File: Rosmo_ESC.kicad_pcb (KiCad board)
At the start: 2 copper layers, 50 x 50 mm, 48 parts, among them J1 M-BUS, J2 USB_C_Receptacle_USB2.0, J3 Conn_01x06_MountingPin, J4 Conn_01x06_MountingPin, J5 Conn_01x03, J6 Conn_01x03, J7 Conn_01x02, U1 STM32G474RET6, U2 PRTR5V0U2F, U3 MPS6540H, U4 MPS6540H

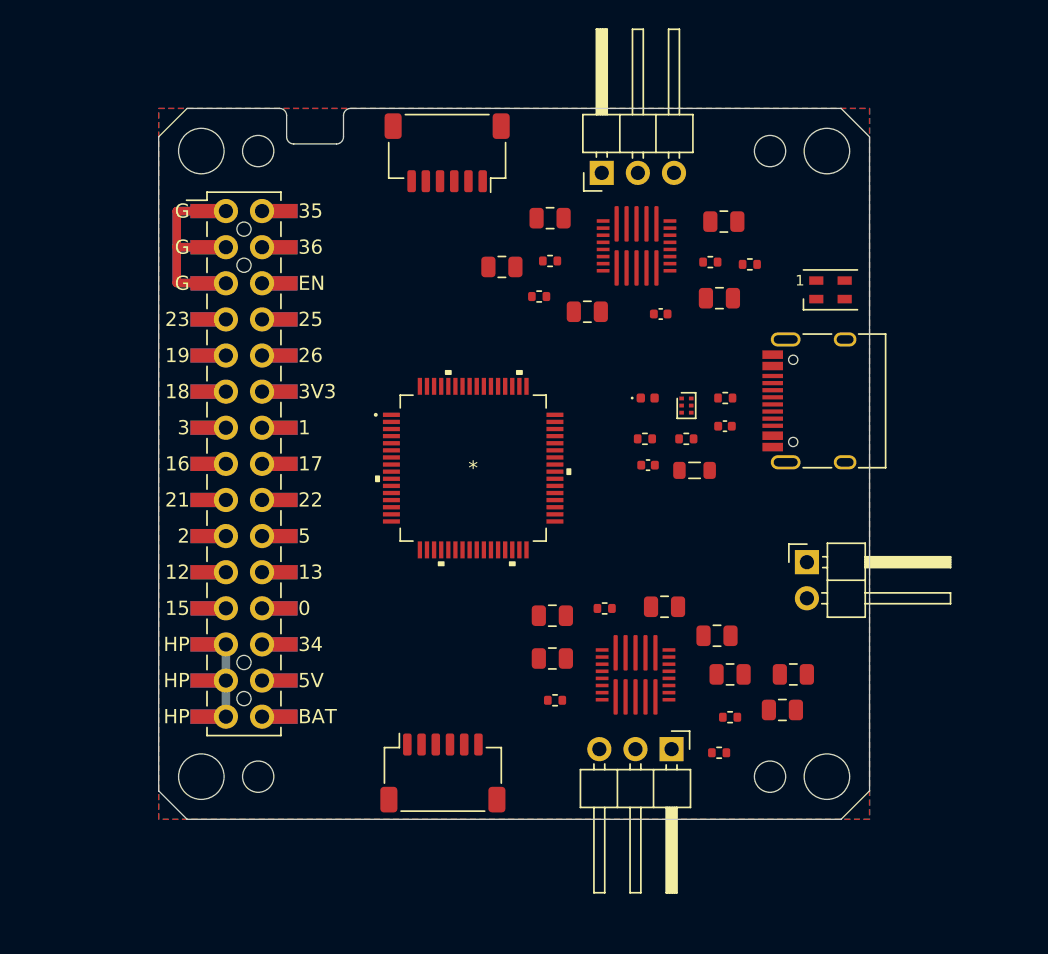
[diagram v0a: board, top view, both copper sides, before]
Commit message: working on rosmo ESC, routing half done
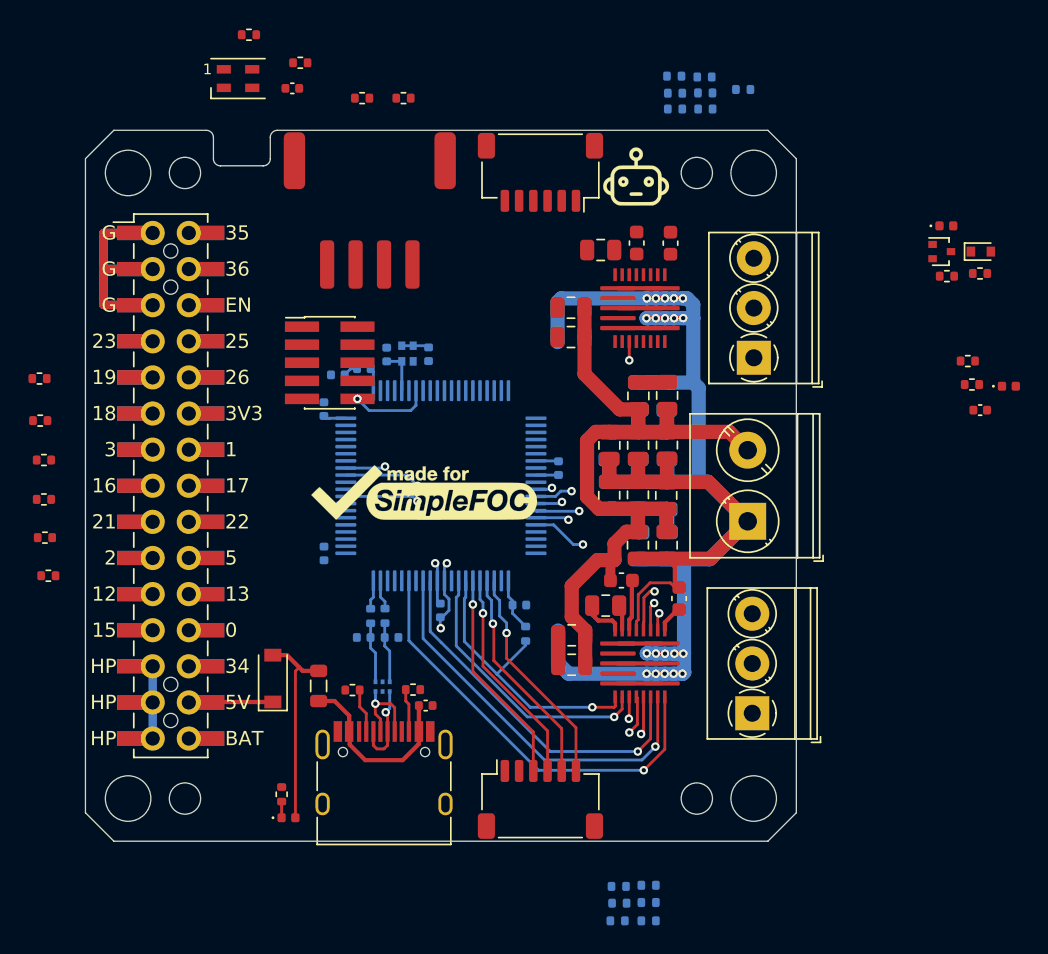
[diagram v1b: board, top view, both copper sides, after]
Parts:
- added C14: 10nF 75V, Capacitor_SMD:C_0805_2012Metric, F.Cu at (84.2, 62.5)
- added C15: 100nF 75V, Capacitor_SMD:C_0805_2012Metric, F.Cu at (84.2, 64.5)
- added C16: 1uF 16V, Capacitor_SMD:C_0603_1608Metric, F.Cu at (88.8, 57.9)
- added C17: 100nF 75V, Capacitor_SMD:C_0805_2012Metric, F.Cu at (86.2, 58.4)
- added C18: 4.7uF 16V, Capacitor_SMD:C_0603_1608Metric, F.Cu at (91.2, 57.9)
- added C19: 10nF 75V, Capacitor_SMD:C_0805_2012Metric, F.Cu at (84.2, 85.5)
- added C20: 100nF 75V, Capacitor_SMD:C_0805_2012Metric, F.Cu at (84.2, 87.6)
- added C21: 1uF 16V, Capacitor_SMD:C_0603_1608Metric, F.Cu at (87.7, 81.7)
- added C22: 100nF 75V, Capacitor_SMD:C_0805_2012Metric, F.Cu at (86.6, 83.4)
- added C23: 4.7uF 16V, Capacitor_SMD:C_0603_1608Metric, F.Cu at (91.8, 82.9)
- added C24: 100nF 6.3V, Capacitor_SMD:C_0402_1005Metric, B.Cu at (74.1, 65.8)
- added C25: 10uF 50V, Capacitor_SMD:C_0805_2012Metric, B.Cu at (90.9, 68.7)
- added C26: 10uF 50V, Capacitor_SMD:C_0805_2012Metric, B.Cu at (88.9, 68.7)
- added C27: 10uF 50V, Capacitor_SMD:C_0805_2012Metric, B.Cu at (86.8, 75.7)
- added C28: 10uF 50V, Capacitor_SMD:C_0805_2012Metric, F.Cu at (88.9, 68.7)
- added C29: 10uF 50V, Capacitor_SMD:C_0805_2012Metric, F.Cu at (90.9, 68.7)
- added C30: 10uF 50V, Capacitor_SMD:C_0805_2012Metric, B.Cu at (90.9, 79.2)
- added C31: 10uF 50V, Capacitor_SMD:C_0805_2012Metric, B.Cu at (90.9, 75.7)
- added C32: 10uF 50V, Capacitor_SMD:C_0805_2012Metric, B.Cu at (88.9, 75.7)
- added C33: 10uF 50V, Capacitor_SMD:C_0805_2012Metric, F.Cu at (86.8, 75.7)
- added C34: 10uF 50V, Capacitor_SMD:C_0805_2012Metric, F.Cu at (88.9, 75.6)
- added C35: 10uF 50V, Capacitor_SMD:C_0805_2012Metric, F.Cu at (90.8, 75.7)
- added C36: 10uF 50V, Capacitor_SMD:C_0805_2012Metric, B.Cu at (88.9, 79.2)
- added C37: 10uF 50V, Capacitor_SMD:C_0805_2012Metric, B.Cu at (86.8, 72.2)
- added C38: 10uF 50V, Capacitor_SMD:C_0805_2012Metric, F.Cu at (88.9, 79.2)
- added C39: 10uF 50V, Capacitor_SMD:C_0805_2012Metric, F.Cu at (90.9, 79.2)
- added C40: 10uF 50V, Capacitor_SMD:C_0805_2012Metric, F.Cu at (90.9, 72.1)
- added C41: 10uF 50V, Capacitor_SMD:C_0805_2012Metric, F.Cu at (88.9, 72.2)
- added C42: 10uF 50V, Capacitor_SMD:C_0805_2012Metric, F.Cu at (86.8, 72.2)
- added C43: 10uF 50V, Capacitor_SMD:C_0805_2012Metric, B.Cu at (88.9, 72.2)
- added C44: 10uF 50V, Capacitor_SMD:C_0805_2012Metric, B.Cu at (90.9, 72.2)
- added D3: green, LED_SMD:LED_0402_1005Metric, F.Cu at (110.5, 56.7)
- added D4: SK6805, LED_SMD:LED_SK6805_PLCC4_2.4x2.7mm_P1.3mm, F.Cu at (60.7, 46.4)
- added D5: SC1333-01ETG, Diode_SMD:D_0402_1005Metric, F.Cu at (115.0, 68.0)
- added D6: 2.84V, Diode_SMD:D_SOD-523, F.Cu at (113.0, 58.5)
- added J8: Conn_01x03, TerminalBlock_Phoenix:TerminalBlock_Phoenix_PT-1,5-3-3.5-H_1x03_P3.50mm_Horizontal, F.Cu at (96.9, 91.0)
- added J9: Conn_01x02, TerminalBlock_Phoenix:TerminalBlock_Phoenix_PT-1,5-2-5.0-H_1x02_P5.00mm_Horizontal, F.Cu at (96.6, 77.5)
- added L1: SimpleFOC_Logo, runger:MadeForSimpleFOC_16mm, F.Cu at (73.8, 75.5)
- added L2: Robo_Logo, runger:Robo_logo2, F.Cu at (88.7, 53.2)
- added L3: Logo_Open_Hardware_Small, Symbol:OSHW-Symbol_6.7x6mm_SilkScreen, B.Cu at (84.9, 95.5)
- added L4: CC_Logo, runger:CC_Logo_5mm, B.Cu at (89.5, 89.0)
- added L5: CC_Attribution_Logo, runger:CC_Attribution_Logo_5mm, B.Cu at (84.9, 89.0)
- added L6: CC_Sharealike_Logo, runger:CC_Sharealike_Logo_5mm, B.Cu at (80.4, 89.0)
- added Q1: BC847BTT1G, Package_TO_SOT_SMD:SOT-416, F.Cu at (110.2, 58.5)
- added R14: 5k1, Resistor_SMD:R_0402_1005Metric, F.Cu at (65.1, 45.2)
- added R15: 300R, Resistor_SMD:R_0402_1005Metric, F.Cu at (61.5, 43.3)
- added R16: 2.2k 1%, Resistor_SMD:R_0402_1005Metric, F.Cu at (112.1, 66.2)
- added R17: 200Ω, Resistor_SMD:R_0402_1005Metric, F.Cu at (110.6, 60.3)
- added R18: 10k, Resistor_SMD:R_0402_1005Metric, B.Cu at (96.3, 47.1)
- added R19: 2k2 0.5%, Resistor_SMD:R_0402_1005Metric, B.Cu at (93.5, 46.2)
- added R20: 2k2 0.5%, Resistor_SMD:R_0402_1005Metric, B.Cu at (93.6, 47.4)
- added R21: 2k2 0.5%, Resistor_SMD:R_0402_1005Metric, B.Cu at (93.6, 48.5)
- added R22: 2k2 0.5%, Resistor_SMD:R_0402_1005Metric, B.Cu at (91.4, 46.2)
- added R23: 2k2 0.5%, Resistor_SMD:R_0402_1005Metric, B.Cu at (91.5, 47.4)
- added R24: 2k2 0.5%, Resistor_SMD:R_0402_1005Metric, B.Cu at (91.5, 48.5)
- added R25: 10k, Resistor_SMD:R_0402_1005Metric, B.Cu at (81.0, 85.4)
- added R26: 2k2 0.5%, Resistor_SMD:R_0402_1005Metric, B.Cu at (89.6, 103.1)
- added R27: 2k2 0.5%, Resistor_SMD:R_0402_1005Metric, B.Cu at (89.6, 104.3)
- added R28: 2k2 0.5%, Resistor_SMD:R_0402_1005Metric, B.Cu at (89.6, 105.6)
- added R29: 2k2 0.5%, Resistor_SMD:R_0402_1005Metric, B.Cu at (87.5, 103.2)
- added R30: 2k2 0.5%, Resistor_SMD:R_0402_1005Metric, B.Cu at (87.5, 104.4)
- added R31: 2k2 0.5%, Resistor_SMD:R_0402_1005Metric, B.Cu at (87.4, 105.6)
- added R32: 2k2, Resistor_SMD:R_0402_1005Metric, F.Cu at (69.5, 47.7)
- added R33: 2k2, Resistor_SMD:R_0402_1005Metric, F.Cu at (72.4, 47.7)
- added X1: 25MHz, Oscillator:Oscillator_SMD_Abracon_ASCO-4Pin_1.6x1.2mm, B.Cu at (72.7, 65.7)
- C1: value 10nF 10V -> 100nF 6.3V; moved to B.Cu
- C10: value 100nF -> 47pF 10V; footprint Capacitor_SMD:C_0805_2012Metric -> Capacitor_SMD:C_0402_1005Metric; moved to B.Cu
- C11: value 1uF -> 10nF 10V; footprint Capacitor_SMD:C_0805_2012Metric -> Capacitor_SMD:C_0402_1005Metric
- C12: value 100nF -> 100nF 6.3V; footprint Capacitor_SMD:C_0805_2012Metric -> Capacitor_SMD:C_0402_1005Metric
- C13: value 4.7uF -> 100nF 50V 5%; footprint Capacitor_SMD:C_0805_2012Metric -> Capacitor_SMD:C_0402_1005Metric
- C2: value 47pF 10V -> 10pF 6.3V 5%; moved to B.Cu
- C3: value 47pF 10V -> 100nF 6.3V; moved to B.Cu
- C4: value 10nF -> 100nF 6.3V; footprint Capacitor_SMD:C_0805_2012Metric -> Capacitor_SMD:C_0402_1005Metric; moved to B.Cu
- C5, C7: value 100nF -> 100nF 6.3V; footprint Capacitor_SMD:C_0805_2012Metric -> Capacitor_SMD:C_0402_1005Metric; moved to B.Cu
- C6: value 1uF -> 100nF 6.3V; footprint Capacitor_SMD:C_0805_2012Metric -> Capacitor_SMD:C_0402_1005Metric; moved to B.Cu
- C8: value 4.7uF -> 100nF 6.3V; footprint Capacitor_SMD:C_0805_2012Metric -> Capacitor_SMD:C_0402_1005Metric; moved to B.Cu
- C9: value 10nF -> 47pF 10V; footprint Capacitor_SMD:C_0805_2012Metric -> Capacitor_SMD:C_0402_1005Metric; moved to B.Cu
- D1: value green -> PMEG40T10ER; footprint LED_SMD:LED_0402_1005Metric -> Diode_SMD:D_SOD-123
- D2: value SK6805 -> green; footprint LED_SMD:LED_SK6805_PLCC4_2.4x2.7mm_P1.3mm -> LED_SMD:LED_0402_1005Metric
- J3: value Conn_01x06_MountingPin -> Conn_01x04_MountingPin; footprint Connector_JST:JST_SH_SM06B-SRSS-TB_1x06-1MP_P1.00mm_Horizontal -> runger:Grove_A2006WF-04A
- J4: value Conn_01x06_MountingPin -> Conn_02x05; footprint Connector_JST:JST_SH_SM06B-SRSS-TB_1x06-1MP_P1.00mm_Horizontal -> Connector_PinHeader_1.27mm:PinHeader_2x05_P1.27mm_Vertical_SMD
- J5, J6: value Conn_01x03 -> JST_SH_SM06B-SRSS-TB_1x06-1MP; footprint Connector_PinHeader_2.54mm:PinHeader_1x03_P2.54mm_Horizontal -> Connector_JST:JST_SH_SM06B-SRSS-TB_1x06-1MP_P1.00mm_Horizontal
- J7: value Conn_01x02 -> Conn_01x03; footprint Connector_PinHeader_2.54mm:PinHeader_1x02_P2.54mm_Horizontal -> TerminalBlock_Phoenix:TerminalBlock_Phoenix_PT-1,5-3-3.5-H_1x03_P3.50mm_Horizontal
- R1, R2: value 27R -> 2k2
- R10: value 10k -> 5k1
- R11, R8: value 1k -> 5k1
- R12: value 1k -> 47k 1%
- R13: value 1k -> 10k; footprint Capacitor_SMD:C_0805_2012Metric -> Resistor_SMD:R_0402_1005Metric
- R3: value 4k7 -> 5k1
- R5: value 5k1 -> 27R; moved to B.Cu
- R6: value 10k -> 27R; moved to B.Cu
- R7: value 1k -> 4k7
- R9: value 1k -> 5k1; footprint Capacitor_SMD:C_0805_2012Metric -> Resistor_SMD:R_0402_1005Metric
- U1: value STM32G474RET6 -> STM32G491MET6; footprint runger:STM32G474RET6 -> Package_QFP:LQFP-80_12x12mm_P0.5mm; moved to B.Cu
- U2: moved to B.Cu
- moved D2 53.2 mm to (64.3, 98.3)
- moved R11 49.0 mm to (47.4, 81.3)
- moved R1 48.4 mm to (47.1, 76.0)
- moved R3 45.2 mm to (47.1, 73.2)
- moved C12 44.9 mm to (64.5, 47.0)
- moved R2 42.8 mm to (47.1, 78.7)
- moved R7 42.0 mm to (63.8, 96.7), turned to 90 degrees
- moved R10 41.8 mm to (46.8, 70.4)
- moved J2 41.6 mm to (71.0, 96.3), turned to 0 degrees
- moved J3 39.9 mm to (70.0, 55.6), turned to 180 degrees
- moved R12 36.8 mm to (112.3, 67.9)
- moved R6 35.6 mm to (71.1, 84.2), turned to -90 degrees
- moved R4 35.6 mm to (46.8, 67.5)
- moved R5 34.5 mm to (70.1, 84.2), turned to -90 degrees
- moved C5 33.8 mm to (75.0, 83.8), turned to 90 degrees
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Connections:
- C1 pad 1: /VUSB -> GND
- C1 pad 2: GND -> VDD
- C10 pad 1: VSS -> /D+
- C11 pad 1: VSS -> /VUSB
- C11 pad 2: VSS -> GND
- C12 pad 1: Net-(C12-Pad1) -> /LED
- C12 pad 2: Net-(C12-Pad2) -> +5V
- C13 pad 1: GND -> /VBAT
- C13 pad 2: Net-(C13-Pad2) -> GND
- C2 pad 1: /D+ -> GND
- C2 pad 2: GND -> /OSCIN
- C3 pad 1: /D- -> GND
- C3 pad 2: GND -> VDD
- C4 pad 1: VSS -> GND
- C4 pad 2: GND -> VDD
- C5 pad 1: VSS -> GND
- C5 pad 2: GND -> VDD
- C6 pad 1: VSS -> GND
- C6 pad 2: VSS -> VDD
- C7 pad 1: Net-(C7-Pad1) -> GND
- C7 pad 2: Net-(C7-Pad2) -> VDD
- C8 pad 2: Net-(C8-Pad2) -> VDD
- C9 pad 1: VSS -> /D-
- D1 pad 1: Net-(D1-Pad1) -> +5V
- D1 pad 2: VBUS -> +5VD
- D2 pad 1: unconnected-(D2-Pad1) -> Net-(D2-Pad1)
- D2 pad 2: unconnected-(D2-Pad2) -> +5VD
- FB1 pad 2: VBUS -> +5VD
- J3 pad 1: unconnected-(J3-Pad1) -> GND
- J3 pad 2: unconnected-(J3-Pad2) -> VDD
- J3 pad 3: unconnected-(J3-Pad3) -> /SDA1
- J3 pad 4: unconnected-(J3-Pad4) -> /SCL1
- J3 pad MP: unconnected-(J3-PadMP) -> GND
- J4 pad 1: unconnected-(J4-Pad1) -> VDD
- J4 pad 2: unconnected-(J4-Pad2) -> /SWDIO
- J4 pad 3: unconnected-(J4-Pad3) -> GND
- J4 pad 4: unconnected-(J4-Pad4) -> /SWCLK
- J4 pad 5: unconnected-(J4-Pad5) -> GND
- J5 pad 1: unconnected-(J5-Pad1) -> GND
- J5 pad 2: unconnected-(J5-Pad2) -> VDD
- J5 pad 3: unconnected-(J5-Pad3) -> /MOSI0
- J6 pad 1: unconnected-(J6-Pad1) -> GND
- J6 pad 2: unconnected-(J6-Pad2) -> VDD
- J6 pad 3: unconnected-(J6-Pad3) -> /MOSI1
- J7 pad 1: unconnected-(J7-Pad1) -> /M0_PHASEU
- J7 pad 2: unconnected-(J7-Pad2) -> /M0_PHASEV
- R1 pad 1: unconnected-(R1-Pad1) -> /GPIO22
- R1 pad 2: /D- -> VDD
- R10 pad 1: +3V3 -> /nCS0
- R10 pad 2: /M1_nFAULT -> VDD
- R11 pad 1: /VREF -> /nCS1
- R11 pad 2: /M1_AOUTU -> VDD
- R12 pad 1: /VREF -> /VBAT
- R12 pad 2: /M1_AOUTU -> VSS
- R13 pad 1: /VREF -> Net-(D6-Pad1)
- R13 pad 2: /M1_AOUTU -> VSS
- R2 pad 1: unconnected-(R2-Pad1) -> /GPIO21
- R2 pad 2: /D+ -> VDD
- R3 pad 1: Net-(D1-Pad1) -> /GPIO2
- R3 pad 2: GND -> VDD
- R4 pad 1: Net-(J2-PadA5) -> /GPIO5
- R4 pad 2: GND -> VDD
- R5 pad 1: Net-(J2-PadB5) -> Net-(R5-Pad1)
- R5 pad 2: GND -> /D+
- R6 pad 1: +3V3 -> Net-(R6-Pad1)
- R6 pad 2: /M0_nFAULT -> /D-
- R7 pad 1: /VREF -> Net-(D2-Pad1)
- R7 pad 2: /M0_AOUTU -> GND
- R8 pad 1: /VREF -> Net-(J2-PadA5)
- R8 pad 2: /M0_AOUTU -> GND
- R9 pad 1: /VREF -> Net-(J2-PadB5)
- R9 pad 2: /M0_AOUTU -> GND
- U1 pad 1: unconnected-(U1-Pad1) -> VDD
- U1 pad 10: unconnected-(U1-Pad10) -> /M0_AOUTV
- U1 pad 11: unconnected-(U1-Pad11) -> /M0_AOUTW
- U1 pad 12: unconnected-(U1-Pad12) -> /GPIO5
- U1 pad 13: unconnected-(U1-Pad13) -> /M1_AOUTU
- U1 pad 14: unconnected-(U1-Pad14) -> /M1_AOUTV
- U1 pad 15: unconnected-(U1-Pad15) -> GND
- U1 pad 16: unconnected-(U1-Pad16) -> VDD
- U1 pad 17: unconnected-(U1-Pad17) -> /M1_AOUTW
- U1 pad 18: unconnected-(U1-Pad18) -> /nCS0
- U1 pad 19: unconnected-(U1-Pad19) -> /SCLK0
- U1 pad 20: unconnected-(U1-Pad20) -> /MISO0
- U1 pad 21: unconnected-(U1-Pad21) -> /MOSI0
- U1 pad 27: unconnected-(U1-Pad27) -> GND
- U1 pad 29: unconnected-(U1-Pad29) -> VDD
- U1 pad 31: unconnected-(U1-Pad31) -> /M0_ENU
- U1 pad 32: unconnected-(U1-Pad32) -> /M0_INU
- U1 pad 33: unconnected-(U1-Pad33) -> /M0_ENV
- U1 pad 34: unconnected-(U1-Pad34) -> /M0_INV
- U1 pad 35: unconnected-(U1-Pad35) -> /M0_ENW
- U1 pad 36: unconnected-(U1-Pad36) -> /M0_INW
- U1 pad 38: unconnected-(U1-Pad38) -> /M0_nSLEEP
- U1 pad 39: unconnected-(U1-Pad39) -> /M0_nFAULT
- U1 pad 40: unconnected-(U1-Pad40) -> GND
- U1 pad 41: unconnected-(U1-Pad41) -> VDD
- U1 pad 42: unconnected-(U1-Pad42) -> /LED
- U1 pad 43: unconnected-(U1-Pad43) -> /nCS1
- U1 pad 44: unconnected-(U1-Pad44) -> /SCLK1
- U1 pad 45: unconnected-(U1-Pad45) -> /MISO1
- U1 pad 46: unconnected-(U1-Pad46) -> /MOSI1
- U1 pad 47: unconnected-(U1-Pad47) -> /M1_nFAULT
- U1 pad 48: unconnected-(U1-Pad48) -> /M1_nSLEEP
- U1 pad 5: unconnected-(U1-Pad5) -> /OSCIN
- U1 pad 50: unconnected-(U1-Pad50) -> GND
- U1 pad 51: unconnected-(U1-Pad51) -> VDD
- U1 pad 52: unconnected-(U1-Pad52) -> /M1_INU
- U1 pad 53: unconnected-(U1-Pad53) -> /M1_INV
- U1 pad 54: unconnected-(U1-Pad54) -> /SCL1
- U1 pad 55: unconnected-(U1-Pad55) -> /M1_INW
- U1 pad 56: unconnected-(U1-Pad56) -> /GPIO21
- U1 pad 57: unconnected-(U1-Pad57) -> /GPIO22
- U1 pad 59: unconnected-(U1-Pad59) -> Net-(R6-Pad1)
- U1 pad 60: unconnected-(U1-Pad60) -> Net-(R5-Pad1)
- U1 pad 61: unconnected-(U1-Pad61) -> GND
- U1 pad 62: unconnected-(U1-Pad62) -> VDD
- U1 pad 63: unconnected-(U1-Pad63) -> /SWDIO
- U1 pad 64: unconnected-(U1-Pad64) -> /SWCLK
- U1 pad 7: unconnected-(U1-Pad7) -> /nRST
- U1 pad 8: unconnected-(U1-Pad8) -> /VBAT
- U1 pad 9: unconnected-(U1-Pad9) -> /M0_AOUTU
- U3 pad 13: /M0_PHASEU -> /M0_PHASEW
- U3 pad 14: Net-(C8-Pad2) -> Net-(C18-Pad2)
- U3 pad 16: /M0_AOUTU -> /M0_AOUTV
- U3 pad 17: /M0_AOUTU -> /M0_AOUTW
- U3 pad 19: VSS -> Net-(C16-Pad2)
- U3 pad 20: Net-(C7-Pad2) -> Net-(C17-Pad1)
- U3 pad 21: Net-(C7-Pad1) -> Net-(C17-Pad2)
- U3 pad 22: /M0_PHASEU -> /M0_PHASEW
- U4 pad 13: /M1_PHASEU -> /M1_PHASEW
- U4 pad 14: Net-(C13-Pad2) -> Net-(C23-Pad2)
- U4 pad 16: /M1_AOUTU -> /M1_AOUTV
- U4 pad 17: /M1_AOUTU -> /M1_AOUTW
- U4 pad 19: VSS -> Net-(C21-Pad2)
- U4 pad 20: Net-(C12-Pad2) -> Net-(C22-Pad1)
- U4 pad 21: Net-(C12-Pad1) -> Net-(C22-Pad2)
- U4 pad 22: /M1_PHASEU -> /M1_PHASEW
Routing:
- net GND: track 30.9 -> 154.5 mm, vias 0 -> 22
- net VSS: track 0.00 -> 67.0 mm
- net /M1_ENV: track 0.00 -> 38.6 mm, vias 0 -> 2
- net /M1_ENW: track 0.00 -> 35.5 mm, vias 0 -> 2
- net /M1_ENU: track 0.00 -> 34.9 mm, vias 0 -> 2
- net /M1_INW: track 0.00 -> 30.3 mm, vias 0 -> 1
- net /M1_INV: track 0.00 -> 27.9 mm, vias 0 -> 1
- net /M1_INU: track 0.00 -> 25.9 mm, vias 0 -> 1
- net /M1_nFAULT: track 0.00 -> 20.7 mm, vias 0 -> 1
- net /M1_nSLEEP: track 0.00 -> 19.5 mm, vias 0 -> 1
- net /nCS1: track 0.00 -> 15.8 mm, vias 0 -> 1
- net /SCLK1: track 0.00 -> 15.5 mm, vias 0 -> 1
- net /MISO1: track 0.00 -> 15.3 mm, vias 0 -> 1
- net /MOSI1: track 0.00 -> 15.1 mm, vias 0 -> 1
- net +5VD: track 0.00 -> 14.4 mm
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- added copper zone on In2.Cu, net GND
- removed copper zone on B.Cu, net GND
- removed copper zone on F.Cu, net GND
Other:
- copper layers 2 -> 4
- board text added: "Do we need this notch?"

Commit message: intial routing done
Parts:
- R3: moved to B.Cu
- moved R15 54.4 mm to (60.1, 97.6), turned to -90 degrees
- moved D4 50.8 mm to (62.2, 97.2), turned to 90 degrees
- moved R14 49.7 mm to (62.0, 94.8), turned to 180 degrees
- moved C12 48.9 mm to (60.1, 95.7), turned to 90 degrees
- moved R11 33.7 mm to (80.8, 86.0), turned to 90 degrees
- moved R10 33.0 mm to (78.6, 61.4)
- moved D5 32.4 mm to (82.7, 71.8)
- moved C13 30.2 mm to (82.7, 70.7), turned to 180 degrees
- moved R16 29.5 mm to (82.7, 69.6)
- moved R12 27.7 mm to (84.7, 69.6)
- moved R28 25.9 mm to (85.3, 80.1), turned to -90 degrees
- moved R13 25.4 mm to (87.9, 56.0), turned to 180 degrees
- moved R31 24.7 mm to (84.2, 81.1), turned to -90 degrees
- moved R18 24.6 mm to (83.7, 68.2), turned to -90 degrees
- moved R19 23.6 mm to (78.5, 64.5), turned to 90 degrees
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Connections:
- C12 pad 1: /LED -> GND
- J3 pad MP: GND -> unconnected-(J3-PadMP)
- J5 pad MP: GND -> unconnected-(J5-PadMP)
- J6 pad MP: GND -> unconnected-(J6-PadMP)
- U1 pad 11: /M0_AOUTW -> /M0_AOUTU
- U1 pad 22: unconnected-(U1-Pad22) -> /M0_nFAULT
- U1 pad 23: unconnected-(U1-Pad23) -> /M0_nSLEEP
- U1 pad 26: unconnected-(U1-Pad26) -> /VBAT
- U1 pad 38: /M0_nSLEEP -> unconnected-(U1-Pad38)
- U1 pad 39: /M0_nFAULT -> unconnected-(U1-Pad39)
- U1 pad 42: /LED -> unconnected-(U1-Pad42)
- U1 pad 58: unconnected-(U1-Pad58) -> /LED
- U1 pad 8: /VBAT -> unconnected-(U1-Pad8)
- U1 pad 9: /M0_AOUTU -> /M0_AOUTW
- U3 pad 4: /M0_ENW -> /M0_ENV
- U3 pad 5: /M0_ENV -> /M0_ENW
- U4 pad 4: /M1_ENW -> /M1_ENV
- U4 pad 5: /M1_ENV -> /M1_ENW
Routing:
- net GND: track 154.5 -> 264.2 mm, vias 22 -> 65
- net VDD: track 13.5 -> 53.8 mm, vias 1 -> 16
- net VSS: track 67.0 -> 106.2 mm, vias 0 -> 13
- net /SCL1: track 0.00 -> 30.6 mm, vias 0 -> 1
- net /GPIO5: track 0.00 -> 27.7 mm, vias 0 -> 1
- net /M1_AOUTU: track 1.23 -> 27.5 mm
- net /LED: track 0.00 -> 26.2 mm, vias 0 -> 1
- net /M0_AOUTW: track 0.00 -> 25.3 mm, vias 0 -> 1
- net /M0_AOUTV: track 0.00 -> 25.0 mm, vias 0 -> 1
- net /M1_AOUTV: track 2.00 -> 26.4 mm
- net /M1_AOUTW: track 3.23 -> 26.3 mm
- net /M0_AOUTU: track 0.00 -> 23.0 mm, vias 0 -> 1
- net /GPIO21: track 0.00 -> 21.9 mm, vias 0 -> 1
- net /GPIO23: track 0.00 -> 20.3 mm
- net /GPIO19: track 0.00 -> 18.6 mm
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- added copper zone on In1.Cu, net VDD

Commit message: updated to KiCad 6
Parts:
- removed L4: CC_Logo, runger:CC_Logo_5mm
- removed L5: CC_Attribution_Logo, runger:CC_Attribution_Logo_5mm
- removed L6: CC_Sharealike_Logo, runger:CC_Sharealike_Logo_5mm
- moved L3 13.9 mm to (71.0, 96.4)
- moved J7 1.71 mm to (95.3, 66.0)
- moved J8 1.71 mm to (95.2, 91.0)
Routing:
- net /M1_PHASEW: track 10.3 -> 8.09 mm
- net /M0_PHASEW: track 10.4 -> 8.21 mm
- net /M0_PHASEV: track 9.56 -> 7.36 mm
- net /M1_PHASEV: track 9.45 -> 7.26 mm
- net /M0_PHASEU: track 10.4 -> 8.23 mm
- net /M1_PHASEU: track 10.3 -> 8.13 mm
- net GND: track 264.2 -> 262.8 mm
- added copper zone on F.Cu, net /M0_PHASEU
- added copper zone on F.Cu, net /M0_PHASEV
- added copper zone on F.Cu, net /M0_PHASEW
- added copper zone on F.Cu, net /M1_PHASEU
- added copper zone on F.Cu, net /M1_PHASEV
- added copper zone on F.Cu, net /M1_PHASEW
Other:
- outline, holes or cut-outs redrawn
- board text added: "6 - 40V"
- board text added: "SWD"
- board text added: "grove I2C"
- board text added: "motor 0"
- board text added: "motor 1"
- board text added: "pwr"
- board text added: "sensor 0"
- board text added: "sensor 1"
- board text added: "status"
- board text added: "usb"
- board text removed: "Do we need this notch?"

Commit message: v1 prototype for production
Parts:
- added C45: 2.2uF 16V, Capacitor_SMD:C_0603_1608Metric, F.Cu at (62.8, 89.2)
- added C46: 2.2uF 16V, Capacitor_SMD:C_0603_1608Metric, F.Cu at (62.8, 86.1)
- added J10: Conn_02x05, Connector_PinHeader_1.27mm:PinHeader_2x05_P1.27mm_Vertical_SMD, F.Cu at (65.0, 80.5)
- added JB1: M-BUS, Connector_PinHeader_2.54mm:PinHeader_2x15_P2.54mm_Vertical_SMD, B.Cu at (56.0, 75.0)
- added R34: 5k1, Resistor_SMD:R_0402_1005Metric, F.Cu at (62.2, 84.8)
- added U5: MIC5524-3.3YMT-T5, runger:TDFN-4-1EP_1x1mm_P0.65mm_EP0.5x0.5mm, F.Cu at (63.6, 87.7)
- J9: footprint TerminalBlock_Phoenix:TerminalBlock_Phoenix_PT-1,5-2-5.0-H_1x02_P5.00mm_Horizontal -> TerminalBlock_Phoenix:TerminalBlock_Phoenix_PT-1,5-2-3.5-H_1x02_P3.50mm_Horizontal
- L1: moved to B.Cu
- moved L1 16.0 mm to (81.5, 89.5), turned to 180 degrees
- moved R4 9.54 mm to (74.6, 79.0), turned to -90 degrees
- moved L2 8.40 mm to (79.2, 78.5)
- moved R1 3.14 mm to (62.6, 75.8), turned to 90 degrees
- moved FB1 3.07 mm to (68.0, 86.4)
- moved D1 2.43 mm to (65.5, 88.0)
- moved L3 1.82 mm to (71.0, 94.6)
- moved J9 1.39 mm to (95.2, 77.4)
- moved R3 1.17 mm to (65.8, 79.8)
- moved R2 0.26 mm to (64.2, 75.8), turned to -90 degrees
- moved J7 0.11 mm to (95.2, 66.0)
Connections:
- R3 pad 1: /GPIO2 -> /nCS2
- R4 pad 1: /GPIO5 -> /WAKE
- U1 pad 12: /GPIO5 -> /WAKE
- U1 pad 65: /GPIO2 -> /nCS2
- U1 pad 70: unconnected-(U1-Pad70) -> /ADDR2
- U1 pad 71: unconnected-(U1-Pad71) -> /ADDR1
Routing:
- net /WAKE: track 0.00 -> 25.5 mm, vias 0 -> 1
- net /BOOT0: track 0.00 -> 21.4 mm, vias 0 -> 2
- net /GPIO5: track 27.7 -> 10.5 mm
- net /ADDR1: track 0.00 -> 15.6 mm, vias 0 -> 2
- net /ADDR2: track 0.00 -> 11.3 mm, vias 0 -> 2
- net VDD: track 53.8 -> 62.6 mm, vias 16 -> 19
- net +5V: track 14.6 -> 21.0 mm
- net /GPIO2: track 15.2 -> 9.08 mm
- net /nCS2: track 0.00 -> 5.63 mm, vias 0 -> 1
- net /LED: track 26.2 -> 21.5 mm
- net GND: track 262.8 -> 265.1 mm, vias 65 -> 67
- net /GPIO21: track 21.9 -> 24.0 mm
- net +5VD: track 14.1 -> 15.9 mm
- net /GPIO22: track 18.0 -> 19.1 mm
- net VSS: track 106.2 -> 105.4 mm
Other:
- board text added: "3v3"
- board text added: "Dual BLDC driver 2x <5A, 6-40V"
- board text added: "addr1"
- board text added: "addr2"
- board text added: "boot0"
- board text added: "gnd"
- board text added: "io2"
- board text added: "io5"
- board text added: "nCS"
- board text added: "nRST"
- board text added: "sensor 0 SPI"
- board text added: "sensor 1 SPI"
- board text added: "swclk"
- board text added: "swdio"
- board text added: "wake"
- board text added: "©2022 runger"
- board text removed: "sensor 0"
- board text removed: "sensor 1"
